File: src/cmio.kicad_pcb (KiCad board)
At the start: 2 copper layers, 72.4 x 36.8 mm, 35 parts, among them J1 USB_OTG, J2 BANK0, J3 USB_OTG, J4 DSI0, J5 CM3Lite, J6 DSI1, J7 TVOUT, J8 BANK1, J9 Micro_SD_Card_TFP09_2_12B, SW1 Reset, U1 ISL91107IR, U2 LD3985M18R, U3 LD3985M28R

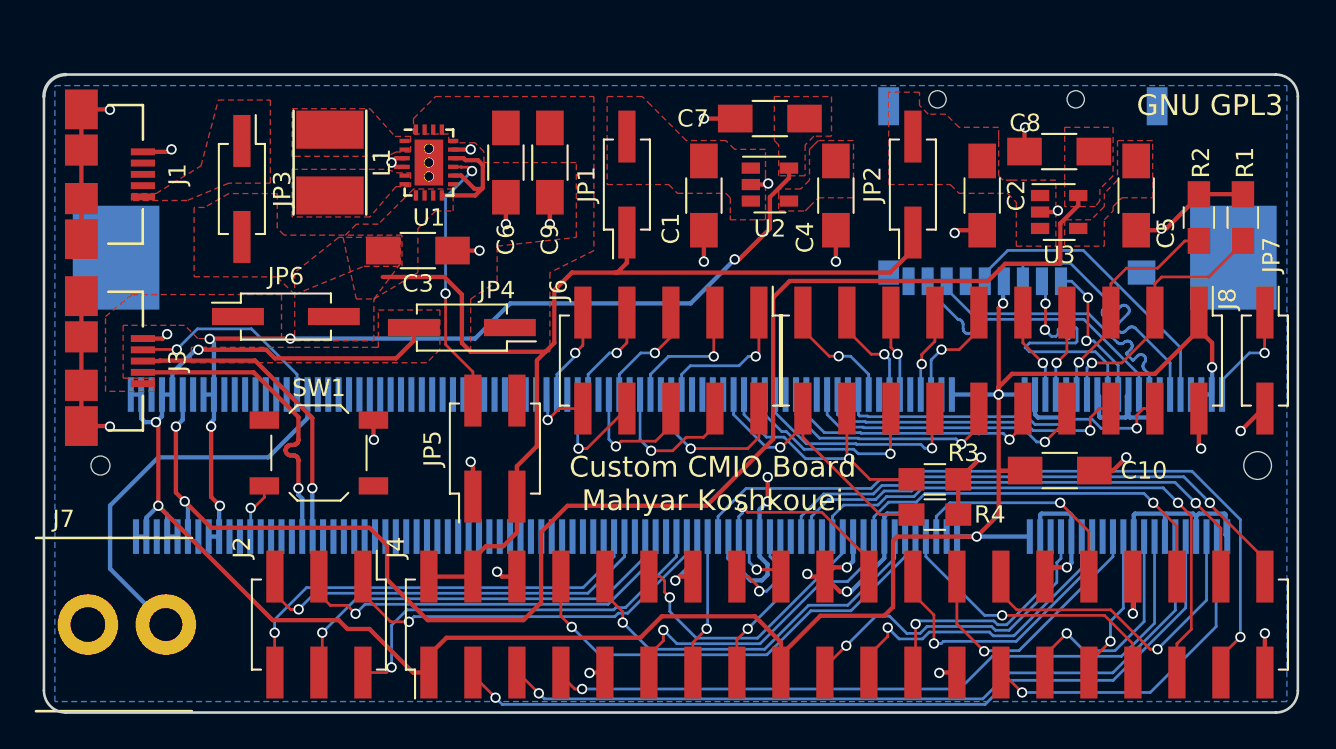
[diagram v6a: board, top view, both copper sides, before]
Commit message: Many Changes
* Add voltage test points. Fixes #10.
* Repositioned components.
* Removed some jumpers.
* Added clearer silkscreen for Reset and TV output. Fixes #8.
* Fixed Micro USB footprints. Fixes #4.

Signed-off-by: Mahyar Koshkouei <deltabeard@users.noreply.github.com>
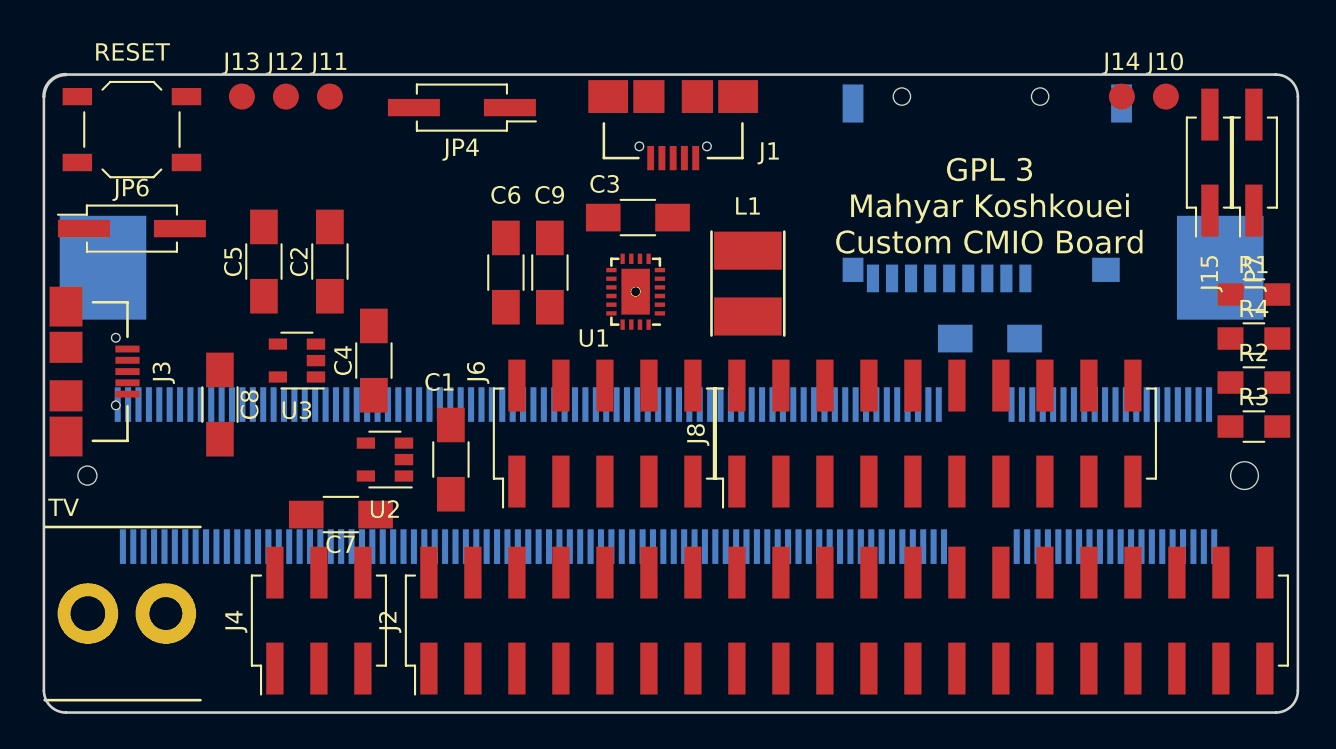
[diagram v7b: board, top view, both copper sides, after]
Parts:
- removed J7: TVOUT, foot:RCA_PHONO
- removed JP1: 1V8 LDO IN, Pin_Headers:Pin_Header_Straight_2x01_Pitch2.54mm_SMD
- removed JP2: 2V8 LDO IN, Pin_Headers:Pin_Header_Straight_2x01_Pitch2.54mm_SMD
- removed JP3: TP, Pin_Headers:Pin_Header_Straight_2x01_Pitch2.54mm_SMD
- removed JP5: EN_Jumper, Pin_Headers:Pin_Header_Straight_2x02_Pitch2.54mm_SMD
- removed SW1: Reset, Buttons_Switches_SMD:SW_SPST_TL3342
- added J10: TEST_5V, Measurement_Points:Measurement_Point_Round-SMD-Pad_Small, F.Cu at (139.7, 50.8)
- added J11: TEST_3V3, Measurement_Points:Measurement_Point_Round-SMD-Pad_Small, F.Cu at (91.4, 50.8)
- added J12: TEST_2V8, Measurement_Points:Measurement_Point_Round-SMD-Pad_Small, F.Cu at (88.9, 50.8)
- added J13: TEST_1V8, Measurement_Points:Measurement_Point_Round-SMD-Pad_Small, F.Cu at (86.4, 50.8)
- added J14: TEST_GND, Measurement_Points:Measurement_Point_Round-SMD-Pad_Small, F.Cu at (137.2, 50.8)
- added J15: CONN_01X02, Pin_Headers:Pin_Header_Straight_2x01_Pitch2.54mm_SMD, F.Cu at (142.2, 54.6)
- added RESET: Reset, Buttons_Switches_SMD:SW_SPST_TL3342, F.Cu at (80.0, 52.7)
- added TV: TVOUT, foot:RCA_PHONO, F.Cu at (77.5, 80.6)
- C10: moved to B.Cu
- J1: value USB_OTG -> USB_POWER
- moved C8 50.6 mm to (85.1, 68.6), turned to 270 degrees
- moved C5 50.5 mm to (87.6, 60.3), turned to 90 degrees
- moved U3 44.8 mm to (89.5, 66.0), turned to 180 degrees
- moved C2 37.8 mm to (91.4, 60.3), turned to 90 degrees
- moved C7 33.7 mm to (92.1, 74.9)
- moved J1 30.6 mm to (111.3, 54.4), turned to 180 degrees
- moved C4 28.3 mm to (94.0, 66.0), turned to 90 degrees
- moved U2 27.3 mm to (94.6, 71.8), turned to 180 degrees
- moved L1 25.1 mm to (115.6, 61.6), turned to 90 degrees
- moved C1 21.1 mm to (98.4, 71.8)
- moved R4 21.0 mm to (144.8, 64.8)
- moved R3 18.7 mm to (144.8, 69.8)
- moved U1 14.1 mm to (109.1, 62.1), turned to 180 degrees
- moved C3 12.8 mm to (109.2, 57.8), turned to 180 degrees
- moved JP4 12.7 mm to (99.1, 51.4)
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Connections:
- C1 pad 1: Net-(C1-Pad1) -> +5V
- C2 pad 1: Net-(C2-Pad1) -> +5V
- J1 pad 1: Net-(J1-Pad1) -> +5V
- U1 pad 13: Net-(JP5-Pad2) -> +5V
- U2 pad 1: Net-(C1-Pad1) -> +5V
- U2 pad 3: Net-(C1-Pad1) -> +5V
- U3 pad 1: Net-(C2-Pad1) -> +5V
- U3 pad 3: Net-(C2-Pad1) -> +5V
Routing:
- net +3V3: track 139.4 -> 0.00 mm, vias 7 -> 0
- net GND: track 132.3 -> 0.00 mm, vias 35 -> 0
- net +2V8: track 83.2 -> 0.00 mm, vias 2 -> 0
- net +5V: track 67.4 -> 0.00 mm
- net +1V8: track 51.9 -> 0.00 mm, vias 5 -> 0
- net /BCM_2: track 48.5 -> 0.00 mm, vias 1 -> 0
- net /BCM_3: track 45.0 -> 0.00 mm, vias 1 -> 0
- net /BCM_26: track 42.8 -> 0.00 mm, vias 1 -> 0
- net /BCM_4: track 41.3 -> 0.00 mm, vias 1 -> 0
- net /BCM_19: track 32.6 -> 0.00 mm, vias 1 -> 0
- net /BCM_21: track 31.9 -> 0.00 mm, vias 1 -> 0
- net /BCM_20: track 29.5 -> 0.00 mm, vias 1 -> 0
- net /BCM_14: track 26.6 -> 0.00 mm, vias 1 -> 0
- net /DSI0_5: track 25.3 -> 0.00 mm, vias 1 -> 0
- net /DSI0_3: track 24.0 -> 0.00 mm, vias 1 -> 0
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- removed copper zone on F.Cu, net +1V8
- removed copper zone on F.Cu, net +2V8
- removed copper zone on F.Cu, net +3V3
- removed copper zone on F.Cu, net +5V
- removed copper zone on B.Cu, net GND
- removed copper zone on F.Cu, net Net-(C1-Pad1)
- removed copper zone on F.Cu, net Net-(C2-Pad1)
- removed copper zone on F.Cu, net Net-(C4-Pad1)
- removed copper zone on F.Cu, net Net-(C5-Pad1)
- removed copper zone on F.Cu, net Net-(C6-Pad2)
- removed copper zone on F.Cu, net Net-(J1-Pad1)
- removed copper zone on F.Cu, net Net-(J3-Pad1)
- removed copper zone on F.Cu, net Net-(L1-Pad1)
- removed copper zone on F.Cu, net Net-(L1-Pad2)
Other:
- board text added: "GPL 3 Mahyar Koshkouei Custom CMIO Board"
- board text removed: "Custom CMIO Board Mahyar Koshkouei"
- board text removed: "GNU GPL3"
- board text removed: "Micro SD"
- board text removed: "Raspberry Pi Compute Module"

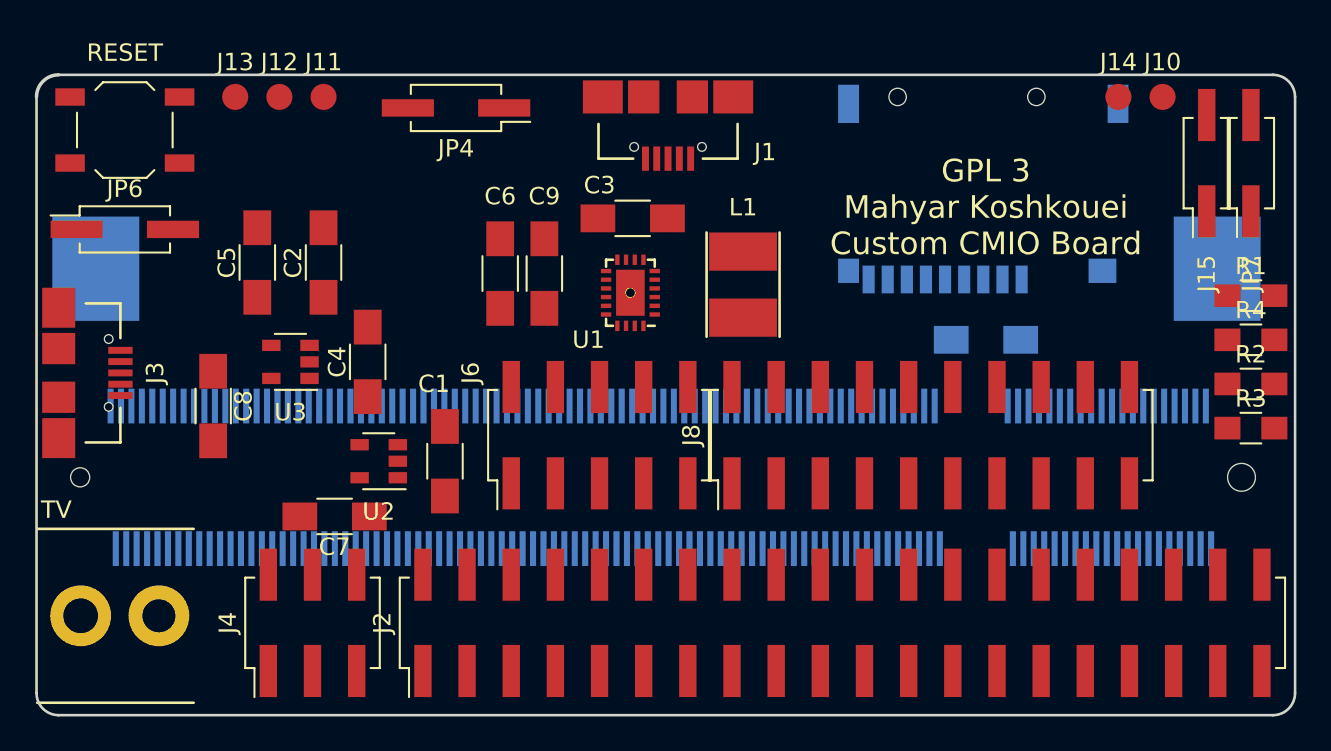
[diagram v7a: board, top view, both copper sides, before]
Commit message: Finish routing
Additionally, added micro USB socket without holes.

Signed-off-by: Mahyar Koshkouei <deltabeard@users.noreply.github.com>
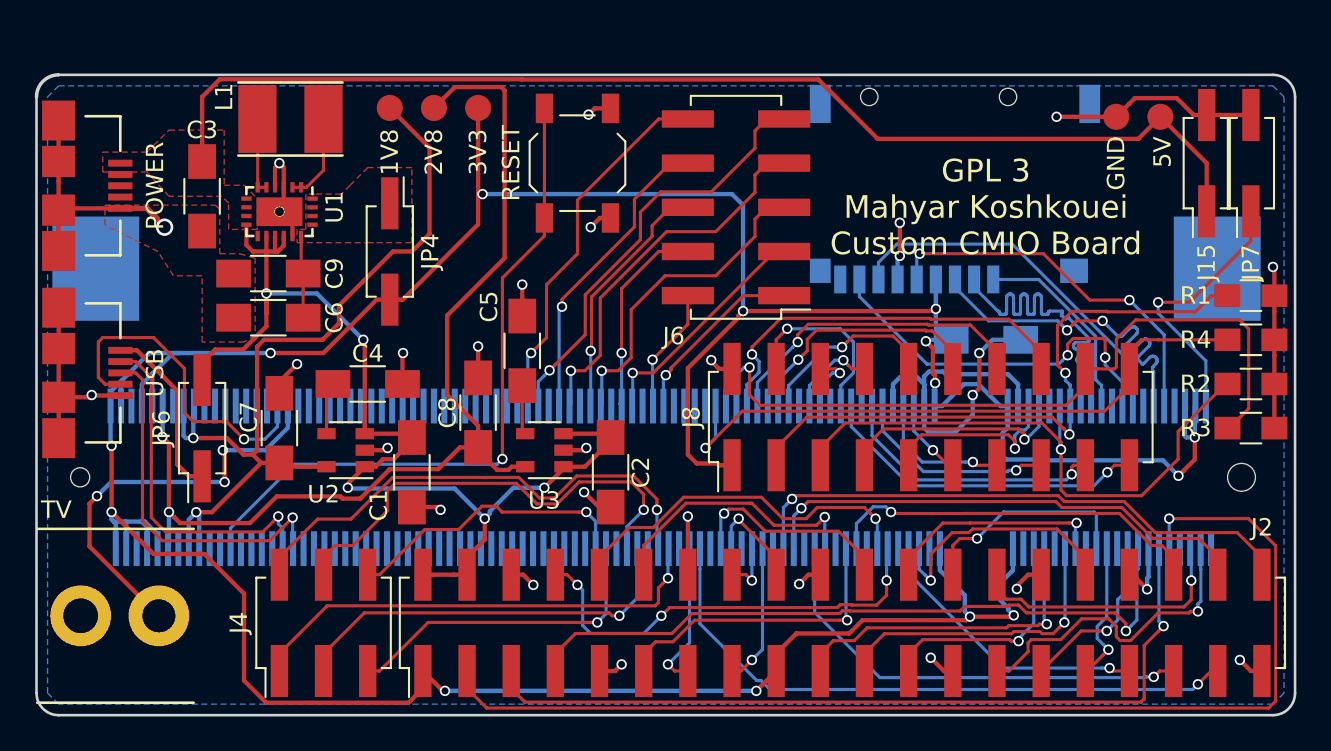
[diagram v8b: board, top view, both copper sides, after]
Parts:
- POWER: renamed from J1; footprint foot:Micro_USB_B_10104110 -> foot:Micro_USB_B_10104110_no_holes
- USB: renamed from J3; footprint foot:Micro_USB_B_10104110 -> foot:Micro_USB_B_10104110_no_holes
- moved POWER 31.5 mm to (79.8, 55.9), turned to 270 degrees
- moved L1 27.7 mm to (89.5, 52.1), turned to 180 degrees
- moved RESET 26.1 mm to (106.0, 54.6), turned to 270 degrees
- moved C3 24.8 mm to (84.5, 56.5), turned to 270 degrees
- moved U1 20.7 mm to (88.9, 57.4), turned to 270 degrees
- moved C2 20.4 mm to (108.0, 72.4), turned to 270 degrees
- moved C5 16.1 mm to (102.9, 65.4)
- moved C9 15.9 mm to (88.3, 61.0), turned to 0 degrees
- moved U3 15.5 mm to (104.1, 71.1)
- moved J6 15.3 mm to (115.2, 57.1), turned to 180 degrees
- moved C8 15.2 mm to (100.3, 69.0), turned to 90 degrees
- moved C6 13.6 mm to (88.3, 63.5), turned to 0 degrees
- moved JP6 12.3 mm to (84.5, 69.8), turned to 90 degrees
- moved JP4 9.09 mm to (95.2, 59.7), turned to 270 degrees
- moved 1V8 8.91 mm to (95.2, 51.4)
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- renumbered J13 to 1V8, J12 to 2V8, J11 to 3V3, J10 to 5V, J14 to GND
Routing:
- net +3V3: track 0.00 -> 208.1 mm, vias 0 -> 14
- net +5V: track 0.00 -> 132.1 mm, vias 0 -> 5
- net GND: track 0.00 -> 117.7 mm, vias 0 -> 28
- net /BCM_2: track 0.00 -> 65.6 mm, vias 0 -> 1
- net +2V8: track 0.00 -> 58.9 mm, vias 0 -> 2
- net +1V8: track 0.00 -> 49.6 mm, vias 0 -> 2
- net /BCM_3: track 0.00 -> 47.0 mm, vias 0 -> 1
- net /BCM_44: track 0.00 -> 43.5 mm, vias 0 -> 1
- net /BCM_4: track 0.00 -> 40.9 mm, vias 0 -> 1
- net Net-(J5-Pad177): track 0.00 -> 39.6 mm, vias 0 -> 1
- net /BCM_45: track 0.00 -> 36.4 mm, vias 0 -> 1
- net /BCM_26: track 0.00 -> 36.1 mm, vias 0 -> 1
- net /BCM_28: track 0.00 -> 36.1 mm, vias 0 -> 2
- net /BCM_29: track 0.00 -> 34.5 mm, vias 0 -> 1
- net /BCM_21: track 0.00 -> 32.6 mm, vias 0 -> 1
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- added copper zone on F.Cu, net +5V
- added copper zone on B.Cu, net GND
- added copper zone on F.Cu, net GND
- added copper zone on F.Cu, net Net-(C6-Pad2)
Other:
- net class Default: trace_width 0.16 -> 0.18
